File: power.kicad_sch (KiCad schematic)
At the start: 58 parts, among them J1 USB-C 5 A, Q1 AON6324, Q2 AON6324, Q3 AON6324, Q4 AON6324, U1 CH224K, U2 MT3608, U3 LP2950-5.0, U4 AMS1117-3.3, U5 IRS2104, U6 IRS2104, U7 LM2903

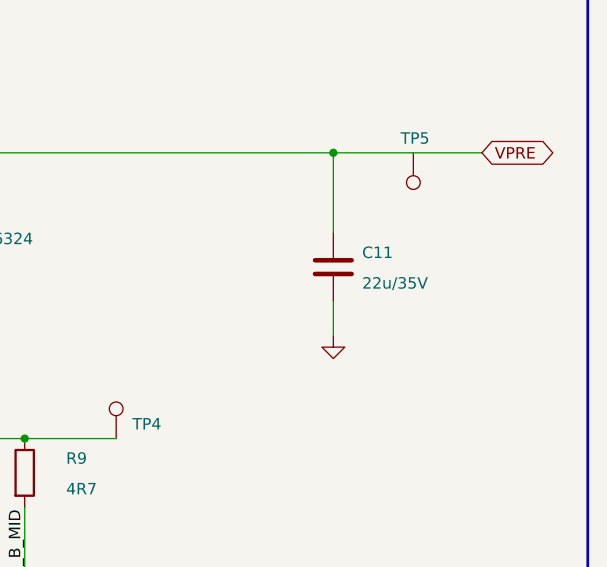
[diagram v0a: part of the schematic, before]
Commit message: v1.2: 0-36 V range, and analogue nets onto real ADC pins
Two changes, one of them serious.

The serious one: ADC_VBUS, ADC_VPRE, ADC_VOUT and ISNS_OUT were on PD2, PD3,
PC6 and PC7.  None of those four pins has an ADC channel on this part, so not
one of the four measurements could ever have been taken.  They move to PA0,
PA1, PA4 and PA5 - ADC_IN0, 1, 4 and 5 - and the timer outputs shuffle to
suit.

The range change: the feedback divider goes from 39k/10k to 150k/10k, which
puts 36 V at the top of the range instead of 20 V, and the divider ratio
becomes exactly 16:1 so the reference maths stays integer.  The pre-regulator
bulk capacitor and the output capacitor go to 63 V parts to match, and the
monitor dividers are rescaled the same way.
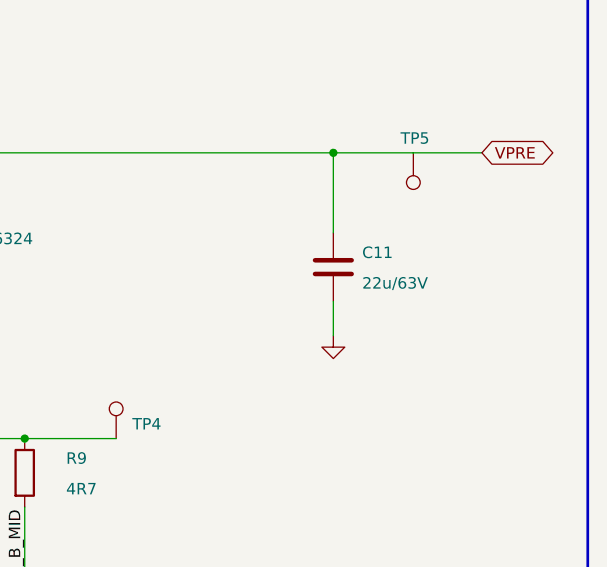
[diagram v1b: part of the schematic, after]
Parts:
- C11: value 22u/35V -> 22u/63V

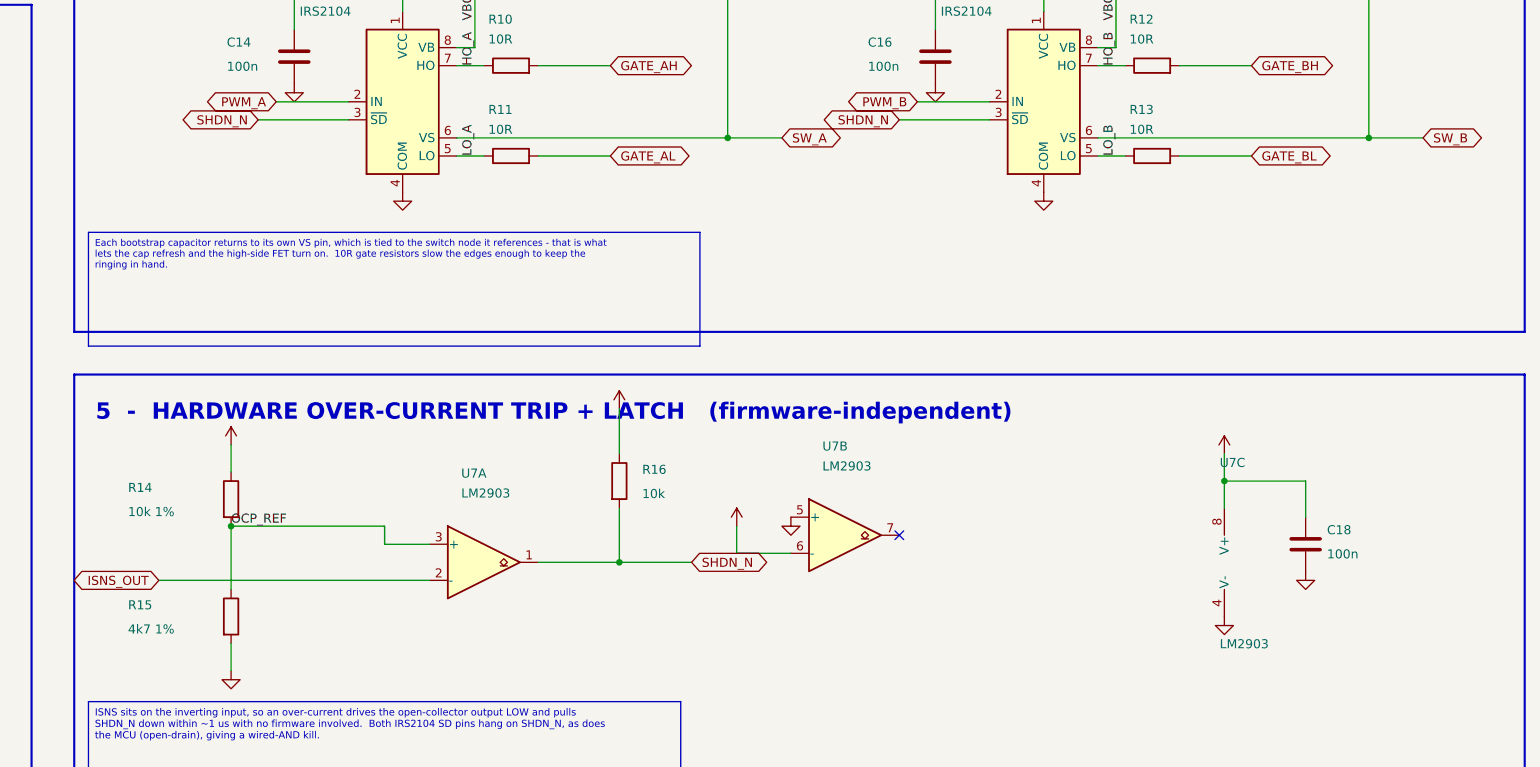
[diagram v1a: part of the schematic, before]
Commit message: v1.3: close the feedback loop, tie the driver returns, rescale the sense chain
Three faults, each of which on its own would have stopped the board working.
All three came out of reading the exported netlist rather than the schematic.

The feedback loop was never closed.  The output divider tap and the error
amplifier's inverting input were two separate nets: the divider went only to an
MCU analogue input, and the amplifier input saw only its compensation
capacitor.  With no DC path around it the amplifier is a bare integrator - its
input floats on bias current and its output ramps to a rail - so the pass
device would have sat hard on or hard off.  The output would not have
regulated; it would have latched.  Both now carry one name and are one node,
which gives V_OUT = 16 x V_REF, exactly what set_ref_dac() already assumes.

The high-side driver returns were open.  Each IRS2104's VS pin sat on a net of
its own instead of on the switch node it references.  VS is what the bootstrap
capacitor and the high-side output float on, so with it open the capacitor
cannot refresh and neither high-side FET switches at all.  Both now tie to the
power switch node.

The current sense saturated at 1.32 A.  0.05 ohm into a gain of 50 is 2.5 V/A,
which reaches the 3.3 V ADC ceiling well below the 3 A the shunt and the pass
device are rated for.  Above that the reading sticks, so the current limit, the
constant-current indicator and the adaptive headroom all stop responding while
the analogue loop carries on delivering current.  0.01 ohm into a gain of 100
gives 1 V/A: full scale 3.3 A, and a fifth of the dissipation in the shunt.

That last change also makes the over-current trip reachable.  At 2.5 V/A a
3.2 A threshold needed 8 V of reference, which the 5 V rail cannot produce, so
the divider had been set to whatever fitted and tripped at 0.64 A.  At 1 V/A
the same threshold needs 3.2 V, and 22k over 39k puts it there.

ERC is clean apart from the library-symbol mismatches that come f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
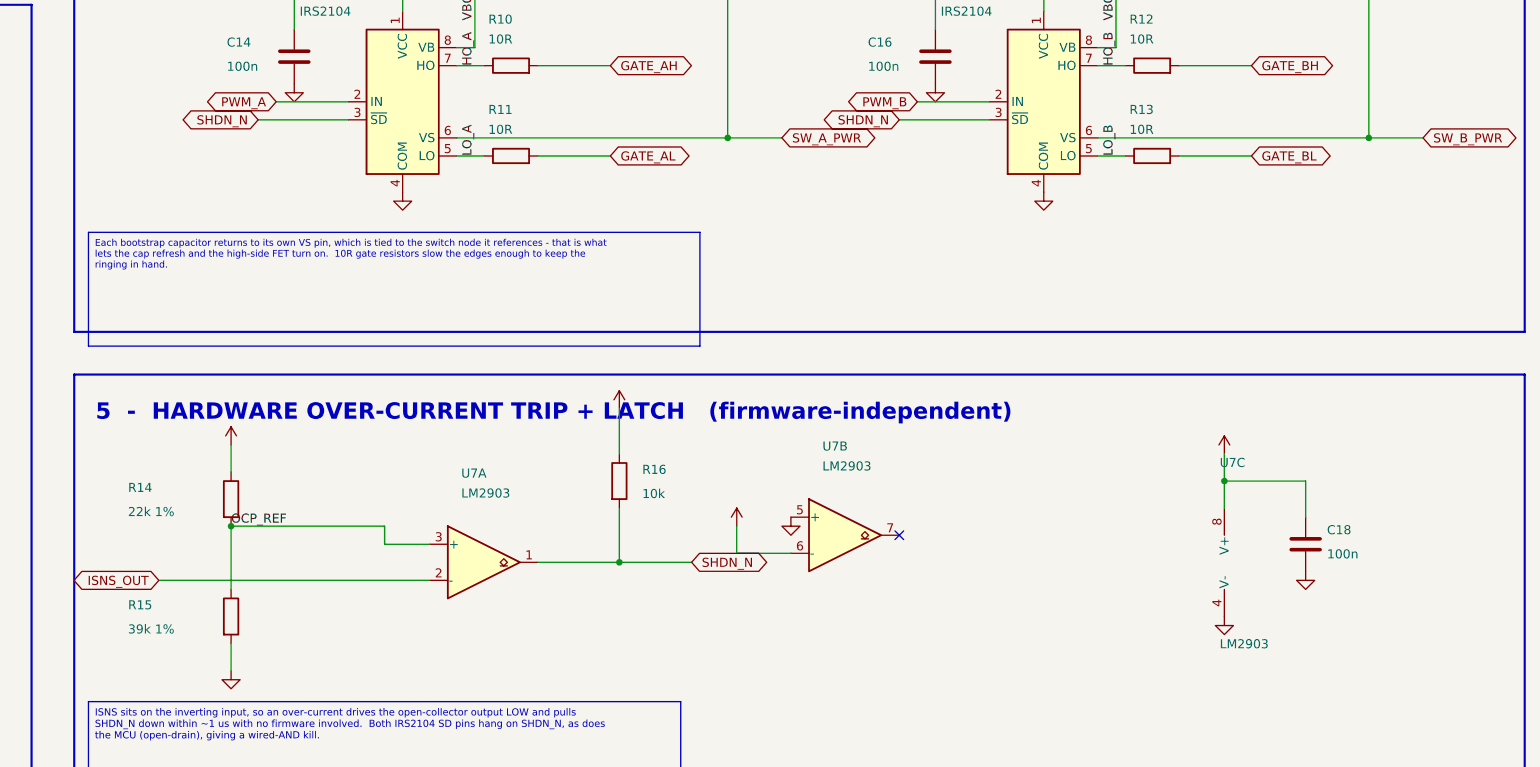
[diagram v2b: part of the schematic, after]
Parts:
- R14: value 10k 1% -> 22k 1%
- R15: value 4k7 1% -> 39k 1%
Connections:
- net SW_A is gone; now on net SW_A_PWR: C15.2, U5.6 (VS)
- net SW_B is gone; now on net SW_B_PWR: C17.2, U6.6 (VS)
